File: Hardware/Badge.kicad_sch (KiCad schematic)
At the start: 65 parts, among them J1 Battery_Conn, J2 Conn_01x02, J3 DEBUG, J4 Conn_02x15_Counter_Clockwise, P1 USB_C_Plug_USB2.0, Q1 SI1967DH-T1-GE3, Q2 2SC4213, SW1 BOOT_MODE, SW2 RESET, SW3 PWR_BATT, SW4 SEL_BATT, SW5 Button B, SW6 Button A, U1 W25Q128JVS, U2 MCP73832-2-OT, U3 LD1117S33TR_SOT223, U4 RP2040, Y1 12MHz_GND24

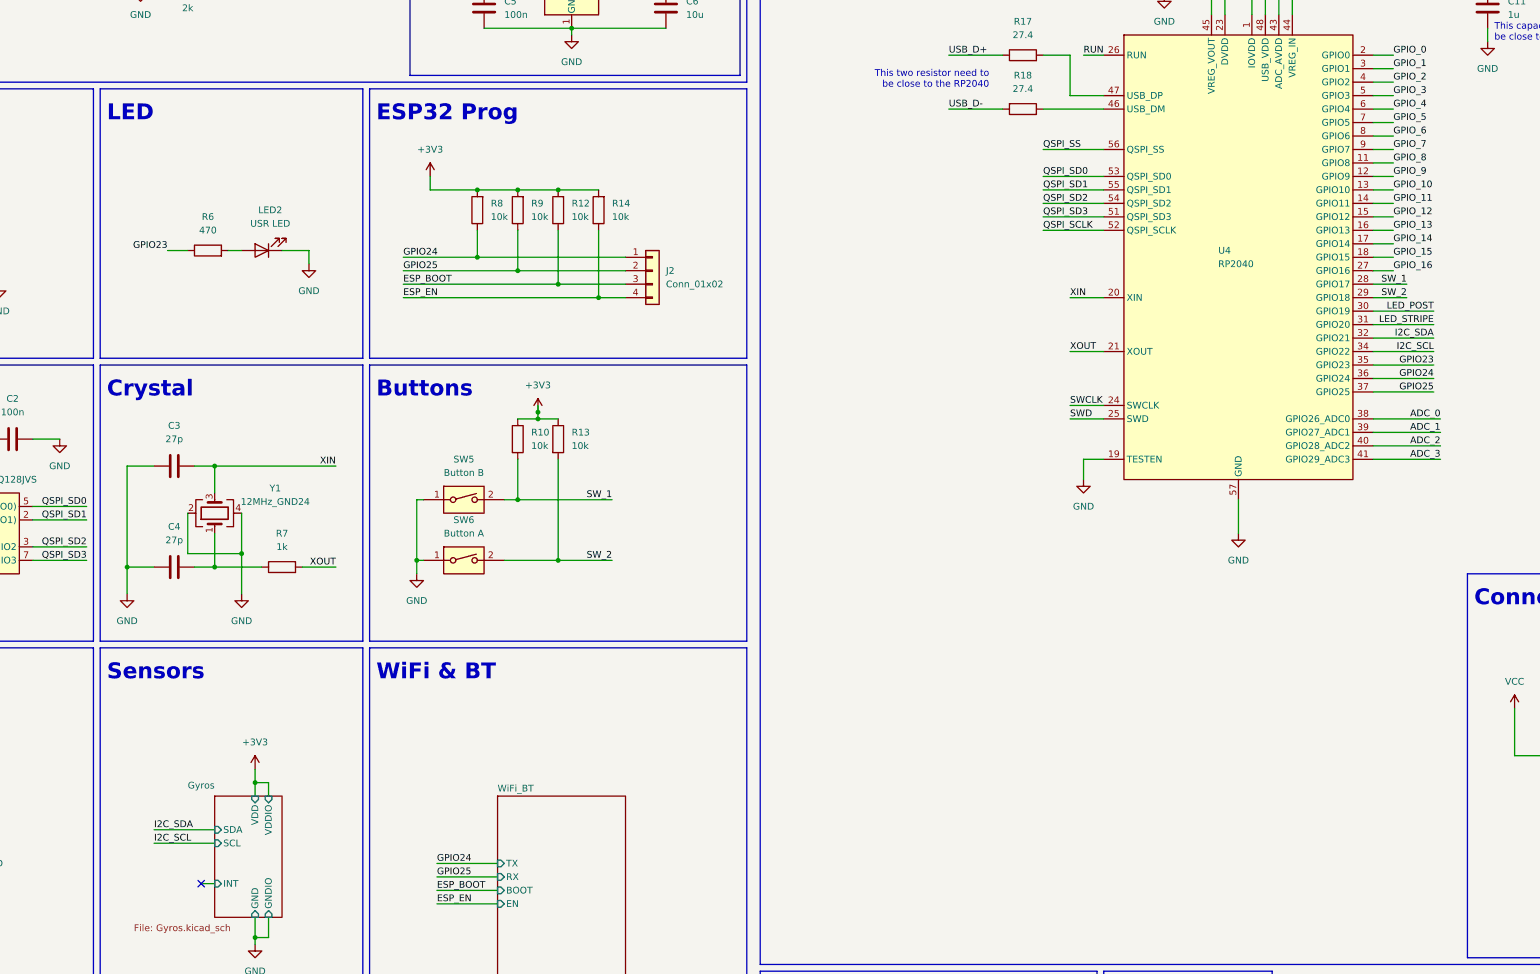
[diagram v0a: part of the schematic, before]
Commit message: Added SAOv2 Connector - re-arranged some RP pins connection
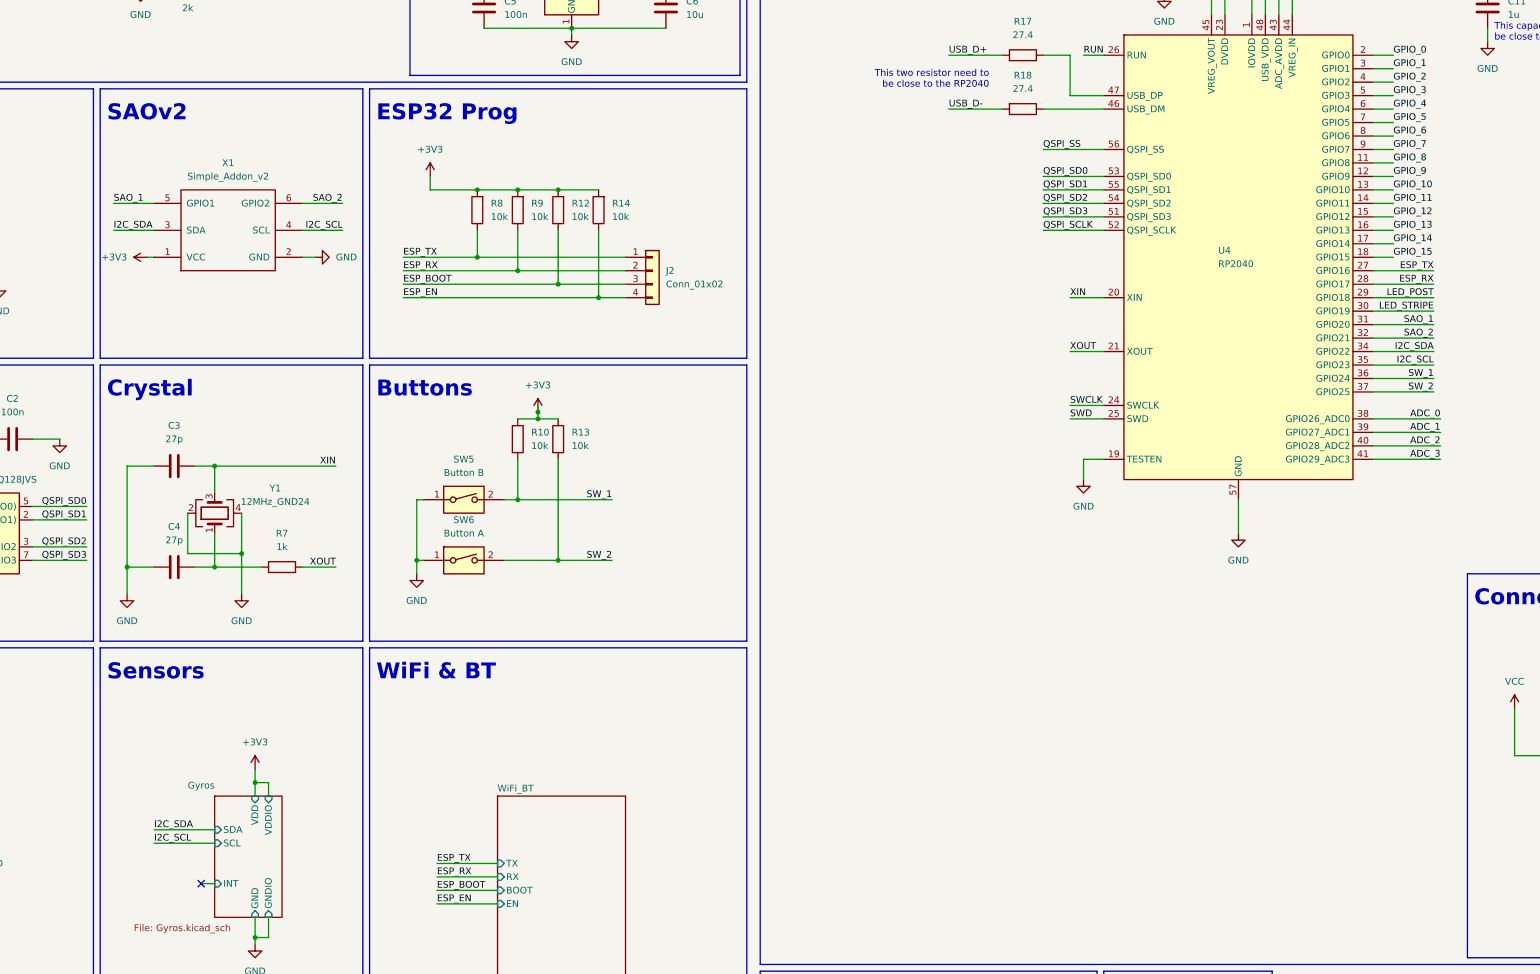
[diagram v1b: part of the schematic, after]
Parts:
- removed LED2: USR LED, LED_SMD:LED_0603_1608Metric, symbol Device:LED
- removed R6: 470, Resistor_SMD:R_0402_1005Metric, symbol Device:R
- added X1: Simple_Addon_v2, SAOv2:Simple_Addon_v2-BADGE-2x3, symbol SAOv2:Simple_Addon_v2
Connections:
- net GPIO23 is gone; now on net I2C_SCL: U4.35 (GPIO23)
- net GPIO_16 is gone; now on net ESP_TX: U4.27 (GPIO16)
- net +3V3: now also X1.1 (VCC)
- net GND: now also X1.2 (GND)
- net I2C_SCL: now also X1.4 (SCL); no longer U4.34 (GPIO22)
- net I2C_SDA: now also U4.34 (GPIO22), X1.3 (SDA); no longer U4.32 (GPIO21)
- net LED_POST: now also U4.29 (GPIO18); no longer U4.30 (GPIO19)
- net LED_STRIPE: now also U4.30 (GPIO19); no longer U4.31 (GPIO20)
- net SW_1: now also U4.36 (GPIO24); no longer U4.28 (GPIO17)
- net SW_2: now also U4.37 (GPIO25); no longer U4.29 (GPIO18)
- net GPIO24 renamed ESP_TX
- net ESP_TX: no longer U4.36 (GPIO24)
- net GPIO25 renamed ESP_RX
- net ESP_RX: now also U4.28 (GPIO17); no longer U4.37 (GPIO25)
- new net SAO_1: U4.31 (GPIO20), X1.5 (GPIO1)
- new net SAO_2: U4.32 (GPIO21), X1.6 (GPIO2)
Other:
- note added: "SAOv2"
- note removed: "LED"

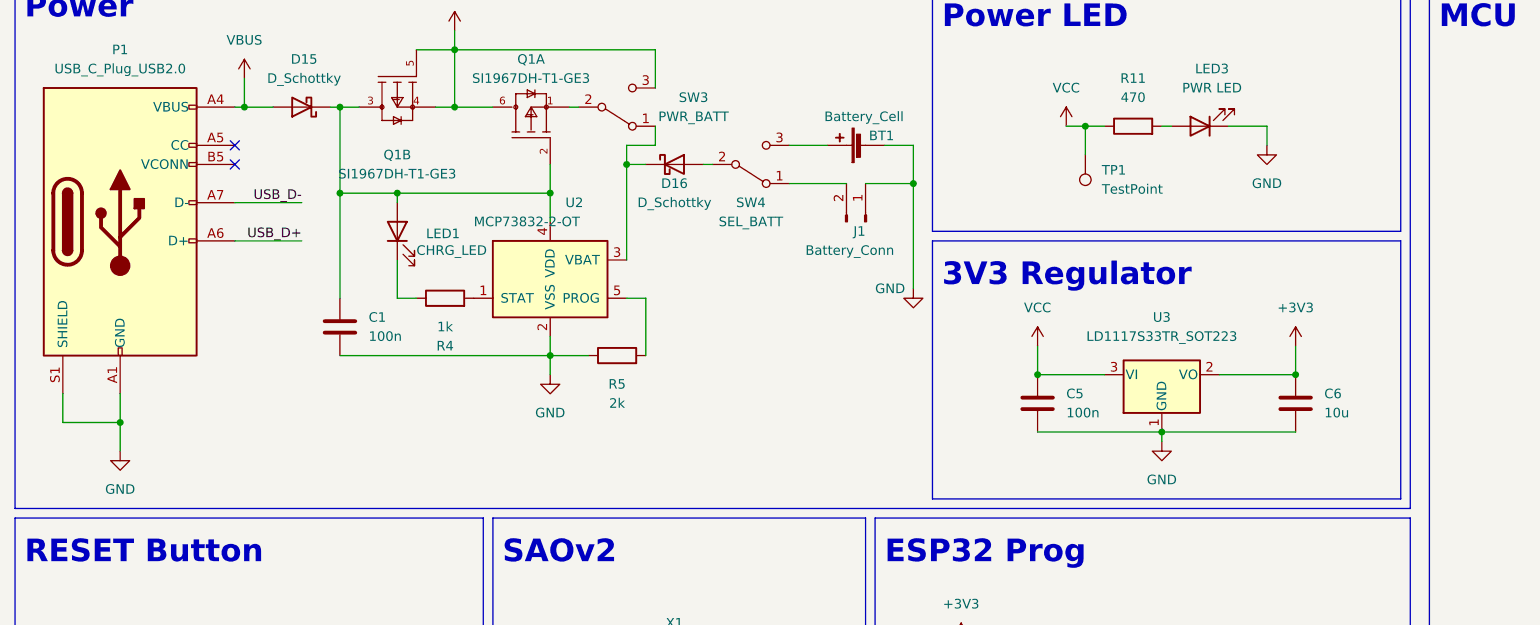
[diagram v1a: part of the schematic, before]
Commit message: Connected both USB-C data signal, moved the crystal - revisisted ready for production
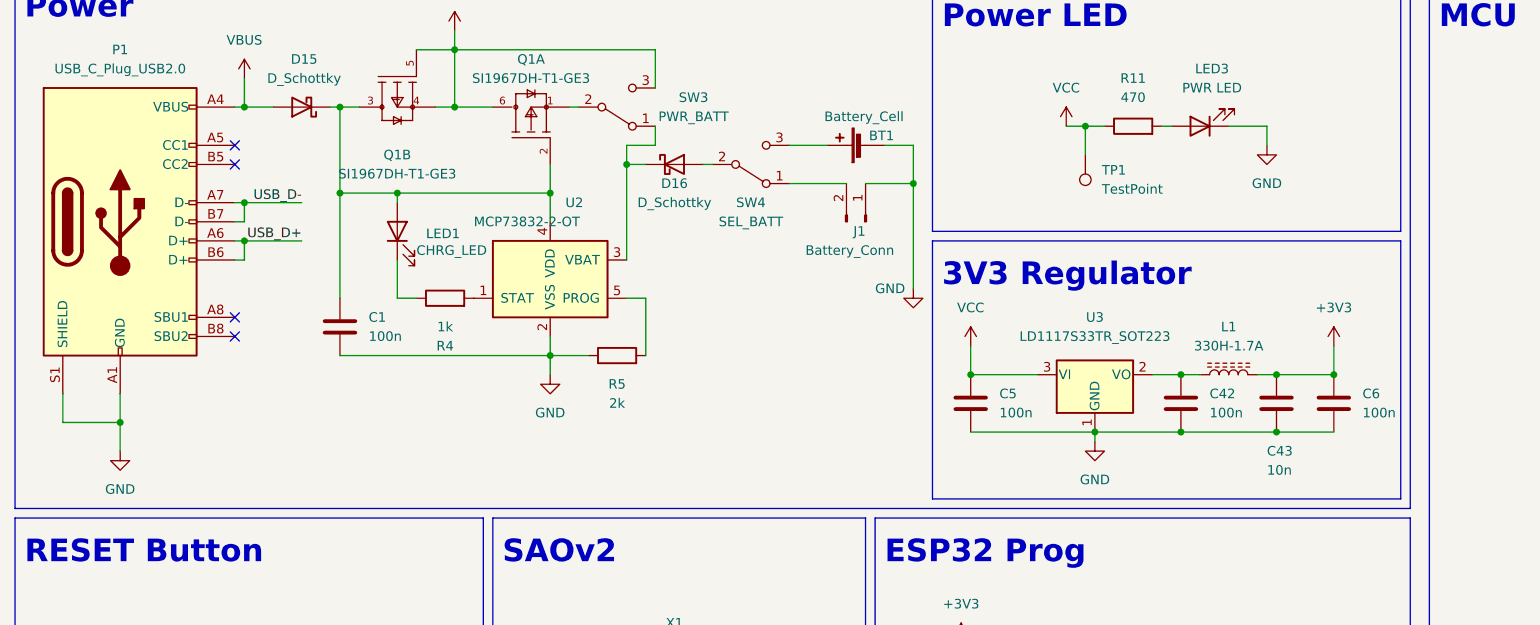
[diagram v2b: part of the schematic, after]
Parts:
- added C42: 100n, Capacitor_SMD:C_0402_1005Metric, symbol Device:C
- added C43: 10n, Capacitor_SMD:C_0402_1005Metric, symbol Device:C
- added L1: 330H-1.7A, Inductor_SMD:L_0603_1608Metric, symbol Device:L_Ferrite
- C6: value 10u -> 100n
- P1: symbol Connector:USB_C_Plug_USB2.0 -> Connector:USB_C_Receptacle_USB2.0
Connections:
- net +3V3: now also C43.2, L1.2; no longer U3.2 (VO)
- net GND: now also C42.1, C43.1
- net USB_D+: now also P1.B6 (D+)
- net USB_D-: now also P1.B7 (D-)
- new net: C42.2, L1.1, U3.2 (VO)
- no-connect marks 5 -> 7
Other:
- moved on the sheet: C5, C6, U3
